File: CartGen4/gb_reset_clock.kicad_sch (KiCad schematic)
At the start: 5 parts, among them U2 SN74LV1T34DCKR

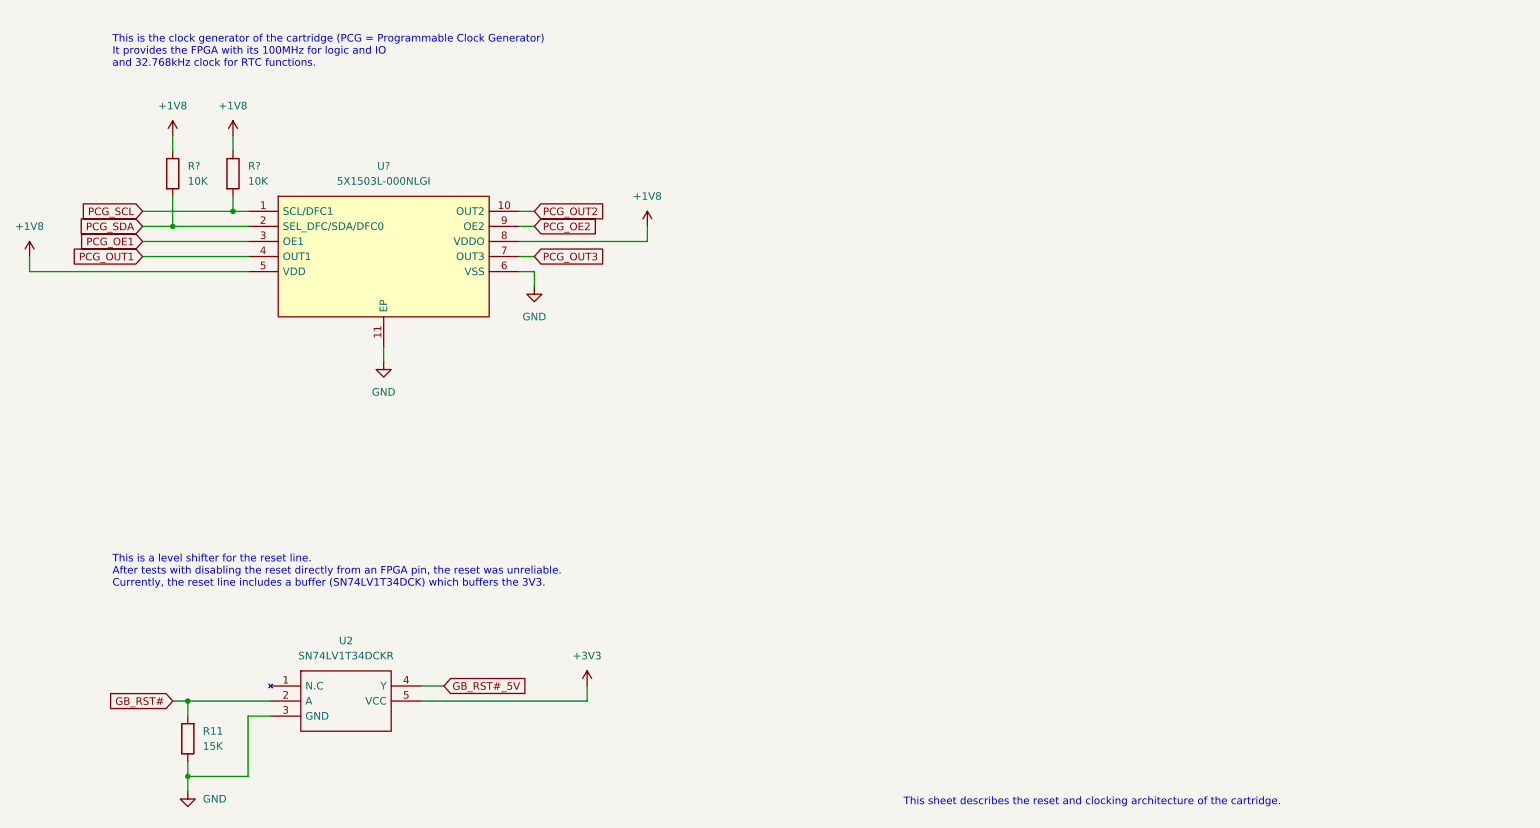
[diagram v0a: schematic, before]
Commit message: Added RTC + Changed clock IC
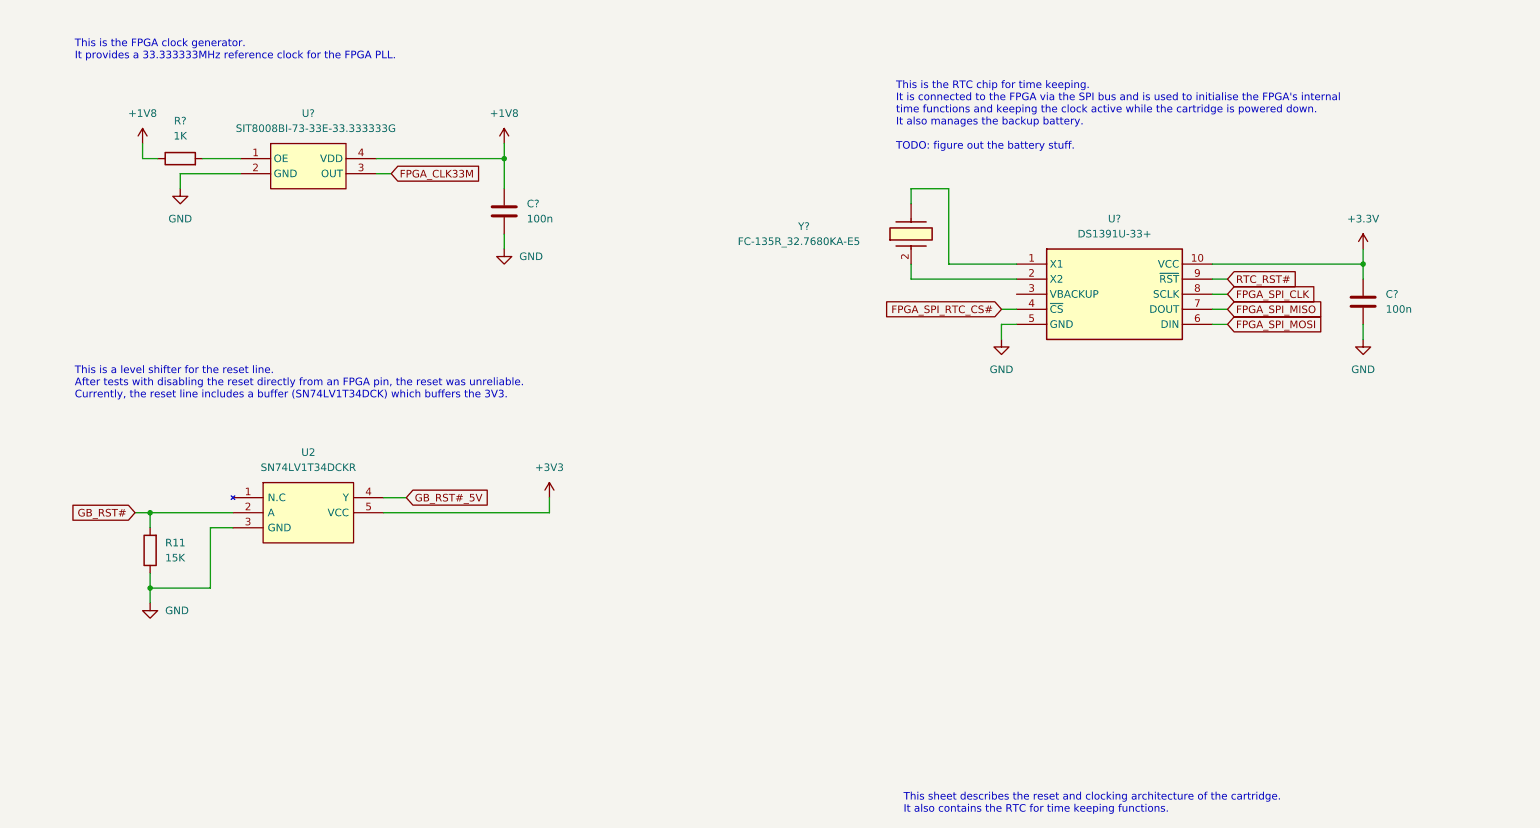
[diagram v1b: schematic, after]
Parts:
- removed R? (x2): 10K, symbol Device:R
- removed U?: 5X1503L-000NLGI, SON40P200X200X110-11N, symbol SamacSys_Parts:5X1503L-000NLGI
- added C? (x2): 100n, symbol Device:C
- added R?: 1K, symbol Device:R
- added U?: DS1391U-33+, symbol SamacSys_Parts:DS1391U-33+
- added U?: SIT8008BI-73-33E-33.333333G, symbol SamacSys_Parts:SIT8008BI-73-33E-33.333333G
- added Y?: FC-135R_32.7680KA-E5, symbol SamacSys_Parts:FC-135R_32.7680KA-E5
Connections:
- net +1V8: now also C?.1, R?.1, U?.4 (VDD)
- net +3V3: now also C?.1, U?.10 (VCC)
- net GND: now also C?.2, C?.2, U?.2 (GND), U?.5 (GND)
- new net: R?.2, U?.1 (OE)
- new net: U?.1 (X1), Y?.
- new net: U?.2 (X2), Y?.2 (CRYSTAL_2)
- new net FPGA_CLK33M: U?.3 (OUT)
- new net FPGA_SPI_CLK: U?.8 (SCLK)
- new net FPGA_SPI_MISO: U?.7 (DOUT)
- new net FPGA_SPI_MOSI: U?.6 (DIN)
- new net FPGA_SPI_RTC_CS#: U?.4 (~{CS})
- new net RTC_RST#: U?.9 (~{RST})
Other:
- note added: "This is the FPGA clock generator. It provides a 33.333333MHz reference clock for the FPGA PLL."
- note added: "This is the RTC chip for time keeping. It is connected to the FPGA via the SPI bus and is used to initialise the FPGA's internal time functions and keeping the clock active while the cartridge is powered down. It also manages the backup battery. TODO: figure out the battery stuff."
- note added: "This sheet describes the reset and clocking architecture of the cartridge. It also contains the RTC for time keeping functions."
- note removed: "This is the clock generator of the cartridge (PCG = Programmable Clock Generator) It provides the FPGA with its 100MHz for logic and IO and 32.768kHz clock for RTC functions."
- note removed: "This sheet describes the reset and clocking architecture of the cartridge."
- title: GB reset and clock -> GB reset and clock + RTC
- moved on the sheet: R11

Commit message: Added SPI flash
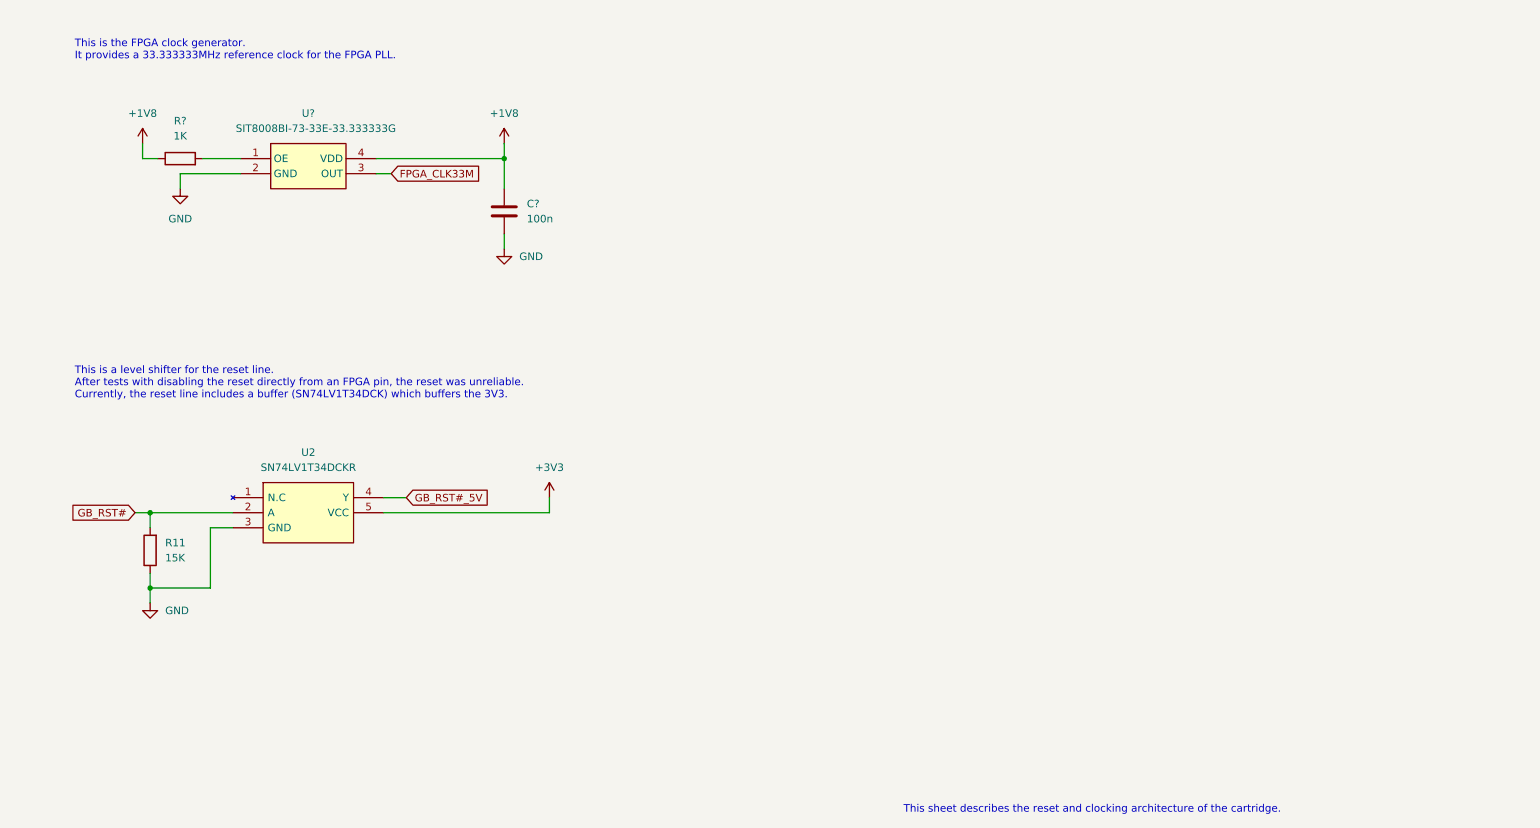
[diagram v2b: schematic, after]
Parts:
- removed C?: 100n, symbol Device:C
- removed U?: DS1391U-33+, symbol SamacSys_Parts:DS1391U-33+
- removed Y?: FC-135R_32.7680KA-E5, symbol SamacSys_Parts:FC-135R_32.7680KA-E5
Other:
- note added: "This sheet describes the reset and clocking architecture of the cartridge."
- note removed: "This is the RTC chip for time keeping. It is connected to the FPGA via the SPI bus and is used to initialise the FPGA's internal time functions and keeping the clock active while the cartridge is powered down. It also manages the backup battery. TODO: figure out the battery stuff."
- note removed: "This sheet describes the reset and clocking architecture of the cartridge. It also contains the RTC for time keeping functions."
- title: GB reset and clock + RTC -> GB reset and clock

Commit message: Added reset button
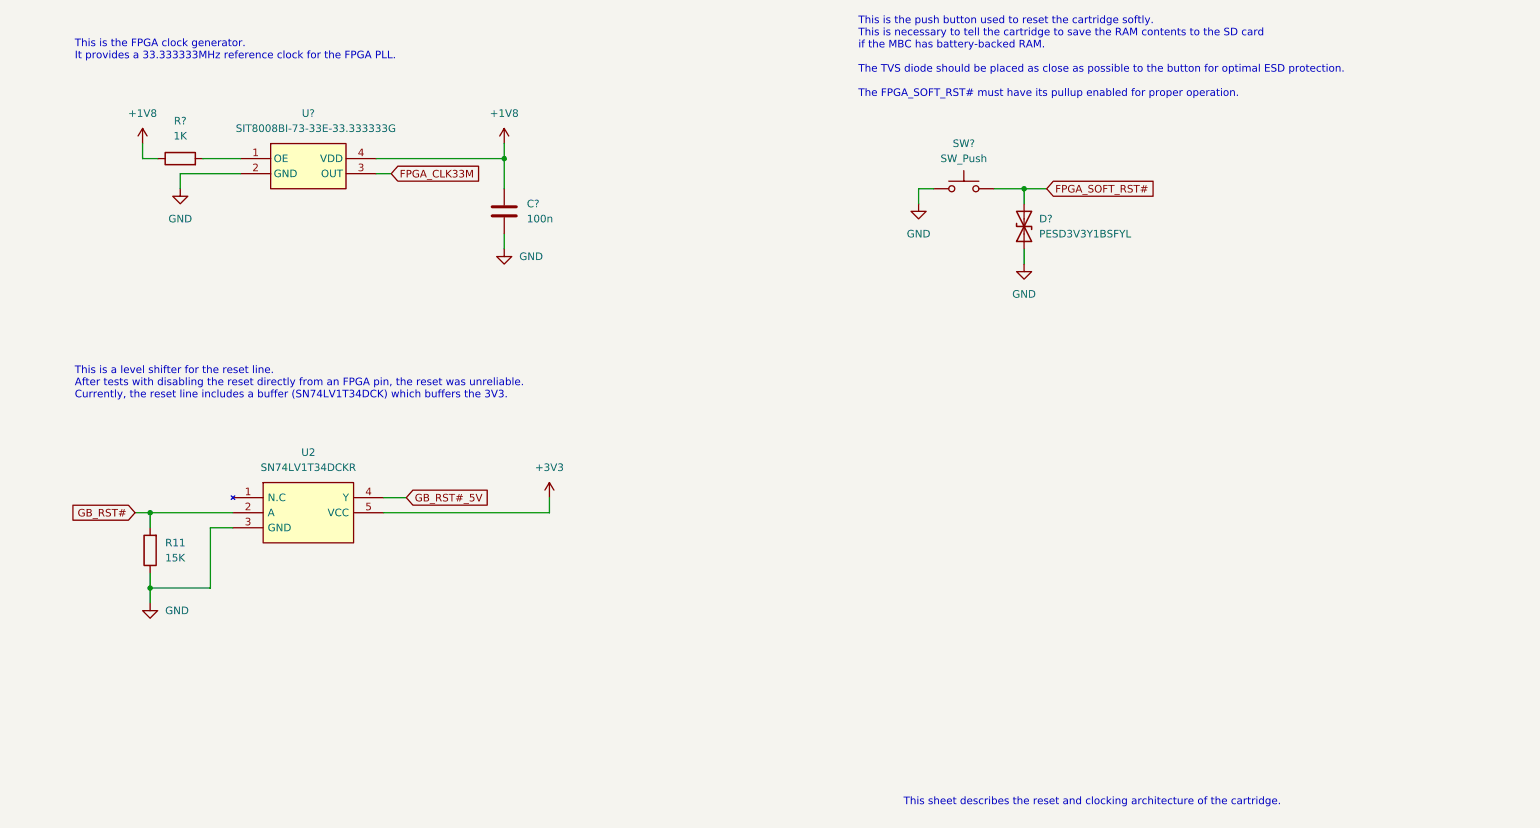
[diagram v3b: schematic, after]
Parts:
- added D?: PESD3V3Y1BSFYL, symbol Device:D_TVS
- added SW?: SW_Push, symbol Switch:SW_Push
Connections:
- net GND: now also D?.1 (A1), SW?.1
- new net FPGA_SOFT_RST#: D?.2 (A2), SW?.2
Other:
- note added: "This is the push button used to reset the cartridge softly. This is necessary to tell the cartridge to save the RAM contents to the SD card if the MBC has battery-backed RAM. The TVS diode should be placed as close as possible to the button for optimal ESD protection. The FPGA_SOFT_RST# must have its pullup enabled for proper operation."
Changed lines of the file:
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@@
     (title "GB reset and clock")
   )
+  (junction (at 199.39 66.04) (diameter 0) (color 0 0 0 0)
+  )
   (junction (at 111.76 60.96) (diameter 0) (color 0 0 0 0)
   )
@@
     (stroke (width 0) (type default) (color 0 0 0 0))
   )
+  (wire (pts (xy 199.39 66.04) (xy 199.39 68.58))
+    (stroke (width 0) (type default) (color 0 0 0 0))
+  )
   (wire (pts (xy 50.8 60.96) (xy 50.8 58.42))
     (stroke (width 0) (type default) (color 0 0 0 0))
   )
+  (wire (pts (xy 199.39 66.04) (xy 203.2 66.04))
+    (stroke (width 0) (type default) (color 0 0 0 0))
+  )
   (wire (pts (xy 119.38 120.65) (xy 119.38 118.11))
     (stroke (width 0) (type default) (color 0 0 0 0))
@@
     (stroke (width 0) (type default) (color 0 0 0 0))
   )
+  (wire (pts (xy 199.39 76.2) (xy 199.39 78.74))
+    (stroke (width 0) (type default) (color 0 0 0 0))
+  )
   (wire (pts (xy 91.44 118.11) (xy 95.25 118.11))
     (stroke (width 0) (type default) (color 0 0 0 0))
@@
     (stroke (width 0) (type default) (color 0 0 0 0))
   )
+  (wire (pts (xy 194.31 66.04) (xy 199.39 66.04))
+    (stroke (width 0) (type default) (color 0 0 0 0))
+  )
   (wire (pts (xy 90.17 60.96) (xy 111.76 60.96))
     (stroke (width 0) (type default) (color 0 0 0 0))
   )
+  (wire (pts (xy 181.61 66.04) (xy 181.61 68.58))
+    (stroke (width 0) (type default) (color 0 0 0 0))
+  )
+  (wire (pts (xy 184.15 66.04) (xy 181.61 66.04))
+    (stroke (width 0) (type default) (color 0 0 0 0))
+  )
   (wire (pts (xy 57.15 63.5) (xy 57.15 66.04))
     (stroke (width 0) (type default) (color 0 0 0 0))
+  )
+  (text "This is the push button used to reset the cartridge softly.\nThis is necessary to tell the cartridge to save the RAM contents to the SD card\nif the MBC has battery-backed RAM.\n\nThe TVS diode should be placed as close as possible to the button for optimal ESD protection.\n\nThe FPGA_SOFT_RST# must have its pullup enabled for proper operation."
+    (at 171.45 50.8 0)
+    (effects (font (size 1.27 1.27)) (justify left bottom))
   )
   (text "This is a level shifter for the reset line.\nAfter tests with disabling the reset directly from an FPGA pin, the reset was unreliable.\nCurrently, the reset line includes a buffer (SN74LV1T34DCK) which buffers the 3V3. "
@@
   )
   (text "This sheet describes the reset and clocking architecture of the cartridge."
-    (at 179.07 171.45 0)
+    (at 179.07 170.18 0)
     (effects (font (size 1.27 1.27)) (justify left bottom))
   )
@@
     (effects (font (size 1.27 1.27)) (justify left))
     (property "Intersheet References" "${INTERSHEET_REFS}" (id 0) (at 109.1536 118.0306 0)
+      (effects (font (size 1.27 1.27)) (justify left) hide)
+    )
+  )
+  (global_label "FPGA_SOFT_RST#" (shape input) (at 203.2 66.04 0) (fields_autoplaced)
+    (effects (font (size 1.27 1.27)) (justify left))
+    (property "Intersheet References" "${INTERSHEET_REFS}" (id 0) (at 221.5788 65.9606 0)
       (effects (font (size 1.27 1.27)) (justify left) hide)
     )
@@
     )
     (pin "1")
+  )
+  (symbol (lib_id "Device:D_TVS") (at 199.39 72.39 90) (unit 1)
+    (in_bom yes) (on_board yes) (fields_autoplaced)
+    (property "Reference" "D?" (id 0) (at 201.93 71.1199 90)
+      (effects (font (size 1.27 1.27)) (justify right))
+    )
+    (property "Value" "PESD3V3Y1BSFYL" (id 1) (at 201.93 73.6599 90)
+      (effects (font (size 1.27 1.27)) (justify right))
+    )
+    (property "Footprint" "" (id 2) (at 199.39 72.39 0)
+      (effects (font (size 1.27 1.27)) hide)
+    )
+    (property "Datasheet" "https://nl.mouser.com/datasheet/2/916/PESD3V3Y1BSF-1370637.pdf" (id 3) (at 199.39 72.39 0)
+      (effects (font (size 1.27 1.27)) hide)
+    )
+    (pin "1")
+    (pin "2")
   )
   (symbol (lib_id "power:GND") (at 57.15 66.04 0) (unit 1)
@@
     (pin "1")
   )
+  (symbol (lib_id "power:GND") (at 181.61 68.58 0) (unit 1)
+    (in_bom yes) (on_board yes) (fields_autoplaced)
+    (property "Reference" "#PWR?" (id 0) (at 181.61 74.93 0)
+      (effects (font (size 1.27 1.27)) hide)
+    )
+    (property "Value" "GND" (id 1) (at 181.61 73.66 0))
+    (property "Footprint" "" (id 2) (at 181.61 68.58 0)
+      (effects (font (size 1.27 1.27)) hide)
+    )
+    (property "Datasheet" "" (id 3) (at 181.61 68.58 0)
+      (effects (font (size 1.27 1.27)) hide)
+    )
+    (pin "1")
+  )
   (symbol (lib_id "SamacSys_Parts:SIT8008BI-73-33E-33.333333G") (at 72.39 58.42 0) (unit 1)
     (in_bom yes) (on_board yes)
@@
     (pin "4")
   )
+  (symbol (lib_id "Switch:SW_Push") (at 189.23 66.04 0) (unit 1)
+    (in_bom yes) (on_board yes) (fields_autoplaced)
+    (property "Reference" "SW?" (id 0) (at 189.23 58.42 0))
+    (property "Value" "SW_Push" (id 1) (at 189.23 60.96 0))
+    (property "Footprint" "" (id 2) (at 189.23 60.96 0)
+      (effects (font (size 1.27 1.27)) hide)
+    )
+    (property "Datasheet" "~" (id 3) (at 189.23 60.96 0)
+      (effects (font (size 1.27 1.27)) hide)
+    )
+    (pin "1")
+    (pin "2")
+  )
+  (symbol (lib_id "power:GND") (at 199.39 78.74 0) (unit 1)
+    (in_bom yes) (on_board yes) (fields_autoplaced)
+    (property "Reference" "#PWR?" (id 0) (at 199.39 85.09 0)
+      (effects (font (size 1.27 1.27)) hide)
+    )
+    (property "Value" "GND" (id 1) (at 199.39 83.82 0))
+    (property "Footprint" "" (id 2) (at 199.39 78.74 0)
+      (effects (font (size 1.27 1.27)) hide)
+    )
+    (property "Datasheet" "" (id 3) (at 199.39 78.74 0)
+      (effects (font (size 1.27 1.27)) hide)
+    )
+    (pin "1")
+  )
   (symbol (lib_id "Device:C") (at 111.76 69.85 0) (unit 1)

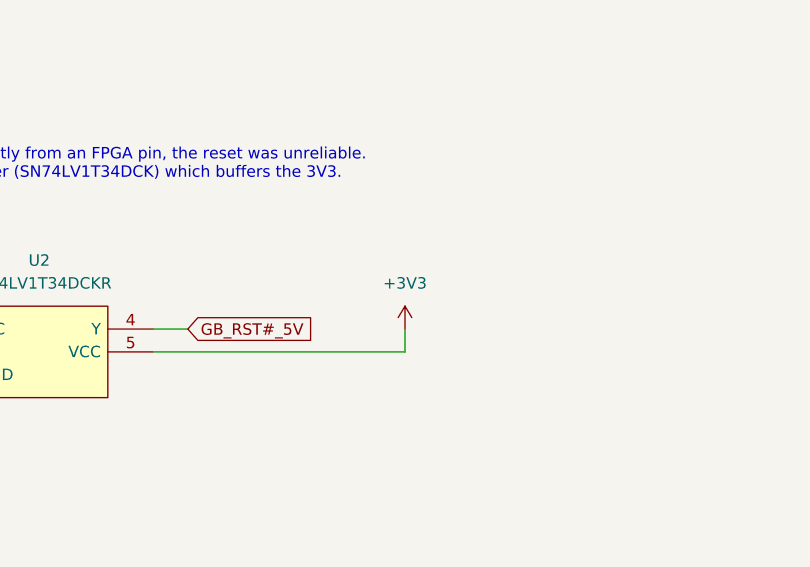
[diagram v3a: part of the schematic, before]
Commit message: Connected and fixed reset
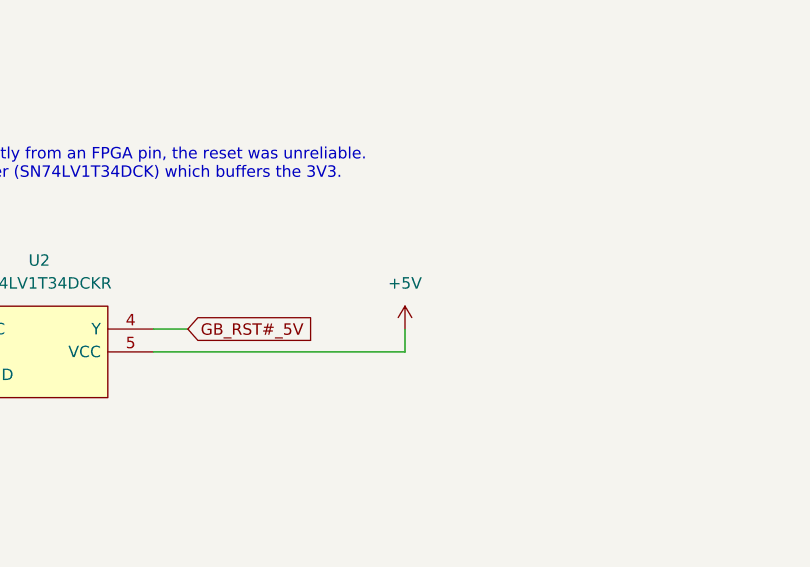
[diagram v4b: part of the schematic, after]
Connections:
- net +3V3 renamed +5V
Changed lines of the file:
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@@
     )
-  )
-  (symbol (lib_id "power:+3V3") (at 119.38 118.11 0) (unit 1)
-    (in_bom yes) (on_board yes) (fields_autoplaced)
-    (property "Reference" "#PWR031" (id 0) (at 119.38 121.92 0)
-      (effects (font (size 1.27 1.27)) hide)
-    )
-    (property "Value" "+3V3" (id 1) (at 119.38 113.03 0))
-    (property "Footprint" "" (id 2) (at 119.38 118.11 0)
-      (effects (font (size 1.27 1.27)) hide)
-    )
-    (property "Datasheet" "" (id 3) (at 119.38 118.11 0)
-      (effects (font (size 1.27 1.27)) hide)
-    )
-    (pin "1")
   )
   (symbol (lib_id "Device:D_TVS") (at 199.39 72.39 90) (unit 1)
@@
     (pin "4")
   )
+  (symbol (lib_id "power:+5V") (at 119.38 118.11 0) (unit 1)
+    (in_bom yes) (on_board yes) (fields_autoplaced)
+    (property "Reference" "#PWR?" (id 0) (at 119.38 121.92 0)
+      (effects (font (size 1.27 1.27)) hide)
+    )
+    (property "Value" "+5V" (id 1) (at 119.38 113.03 0))
+    (property "Footprint" "" (id 2) (at 119.38 118.11 0)
+      (effects (font (size 1.27 1.27)) hide)
+    )
+    (property "Datasheet" "" (id 3) (at 119.38 118.11 0)
+      (effects (font (size 1.27 1.27)) hide)
+    )
+    (pin "1")
+  )
   (symbol (lib_id "Switch:SW_Push") (at 189.23 66.04 0) (unit 1)

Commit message: Added copyright
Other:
- company: (none) -> © Elijah Almeida Coimbra
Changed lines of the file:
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@@
   (title_block
     (title "GB reset and clock")
+    (company "© Elijah Almeida Coimbra")
   )
   (junction (at 199.39 66.04) (diameter 0) (color 0 0 0 0)
